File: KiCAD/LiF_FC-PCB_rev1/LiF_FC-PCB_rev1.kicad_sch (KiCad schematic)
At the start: 0 parts

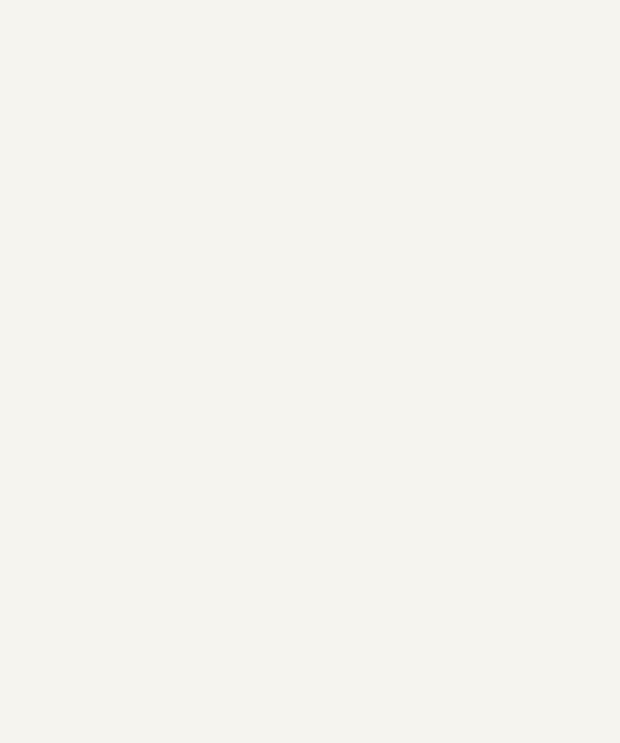
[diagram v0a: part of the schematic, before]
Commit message: merged and fixed Rita's CAN and Load Cell schematics
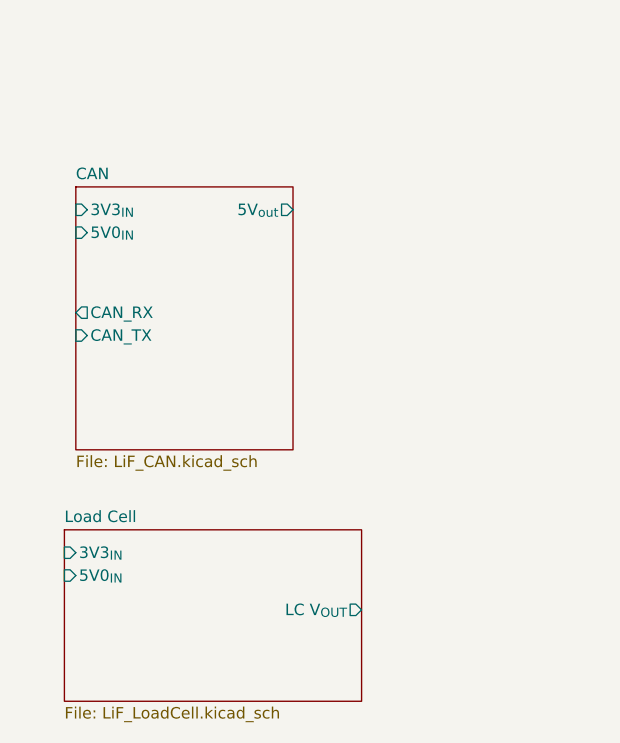
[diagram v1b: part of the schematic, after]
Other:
- added sheet CAN (LiF_CAN.kicad_sch)
- added sheet Load Cell (LiF_LoadCell.kicad_sch)
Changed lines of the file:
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@@
 	(paper "A4")
+	(sheet
+		(at 67.31 171.45)
+		(size 33.02 19.05)
+		(exclude_from_sim no)
+		(in_bom yes)
+		(on_board yes)
+		(dnp no)
+		(fields_autoplaced yes)
+		(stroke
+			(width 0.1524)
+			(type solid)
+		)
+		(fill
+			(color 0 0 0 0.0000)
+		)
+		(property "Sheetname" "Load Cell"
+			(at 67.31 170.7384 0)
+			(effects
+				(font
+					(size 1.27 1.27)
+				)
+				(justify left bottom)
+			)
+		)
+		(property "Sheetfile" "LiF_LoadCell.kicad_sch"
+			(at 67.31 191.0846 0)
+			(effects
+				(font
+					(size 1.27 1.27)
+				)
+				(justify left top)
+			)
+		)
+		(pin "3V3_{IN}" input
+			(at 67.31 173.99 180)
+			(effects
+				(font
+					(size 1.27 1.27)
+				)
+				(justify left)
+			)
+		)
+		(pin "5V0_{IN}" input
+			(at 67.31 176.53 180)
+			(effects
+				(font
+					(size 1.27 1.27)
+				)
+				(justify left)
+			)
+		)
+		(pin "LC V_{OUT}" output
+			(at 100.33 180.34 0)
+			(effects
+				(font
+					(size 1.27 1.27)
+				)
+				(justify right)
+			)
+		)
+		(instances
+			(project "LiF_FC-PCB_rev1"
+				(path "/9e3e8da7-e506-46c9-90e5-307e4ad30d29"
+					(page "7")
+				)
+			)
+		)
+	)
+	(sheet
+		(at 68.58 133.35)
+		(size 24.13 29.21)
+		(exclude_from_sim no)
+		(in_bom yes)
+		(on_board yes)
+		(dnp no)
+		(fields_autoplaced yes)
+		(stroke
+			(width 0.1524)
+			(type solid)
+		)
+		(fill
+			(color 0 0 0 0.0000)
+		)
+		(property "Sheetname" "CAN"
+			(at 68.58 132.6384 0)
+			(effects
+				(font
+					(size 1.27 1.27)
+				)
+				(justify left bottom)
+			)
+		)
+		(property "Sheetfile" "LiF_CAN.kicad_sch"
+			(at 68.58 163.1446 0)
+			(effects
+				(font
+					(size 1.27 1.27)
+				)
+				(justify left top)
+			)
+		)
+		(pin "3V3_{IN}" input
+			(at 68.58 135.89 180)
+			(effects
+				(font
+					(size 1.27 1.27)
+				)
+				(justify left)
+			)
+		)
+		(pin "5V0_{IN}" input
+			(at 68.58 138.43 180)
+			(effects
+				(font
+					(size 1.27 1.27)
+				)
+				(justify left)
+			)
+		)
+		(pin "5V_{out}" output
+			(at 92.71 135.89 0)
+			(effects
+				(font
+					(size 1.27 1.27)
+				)
+				(justify right)
+			)
+		)
+		(pin "CAN_RX" output
+			(at 68.58 147.32 180)
+			(effects
+				(font
+					(size 1.27 1.27)
+				)
+				(justify left)
+			)
+		)
+		(pin "CAN_TX" input
+			(at 68.58 149.86 180)
+			(effects
+				(font
+					(size 1.27 1.27)
+				)
+				(justify left)
+			)
+		)
+		(instances
+			(project "LiF_FC-PCB_rev1"
+				(path "/9e3e8da7-e506-46c9-90e5-307e4ad30d29"
+					(page "6")
+				)
+			)
+		)
+	)
 	(sheet
 		(at 193.04 100.33)

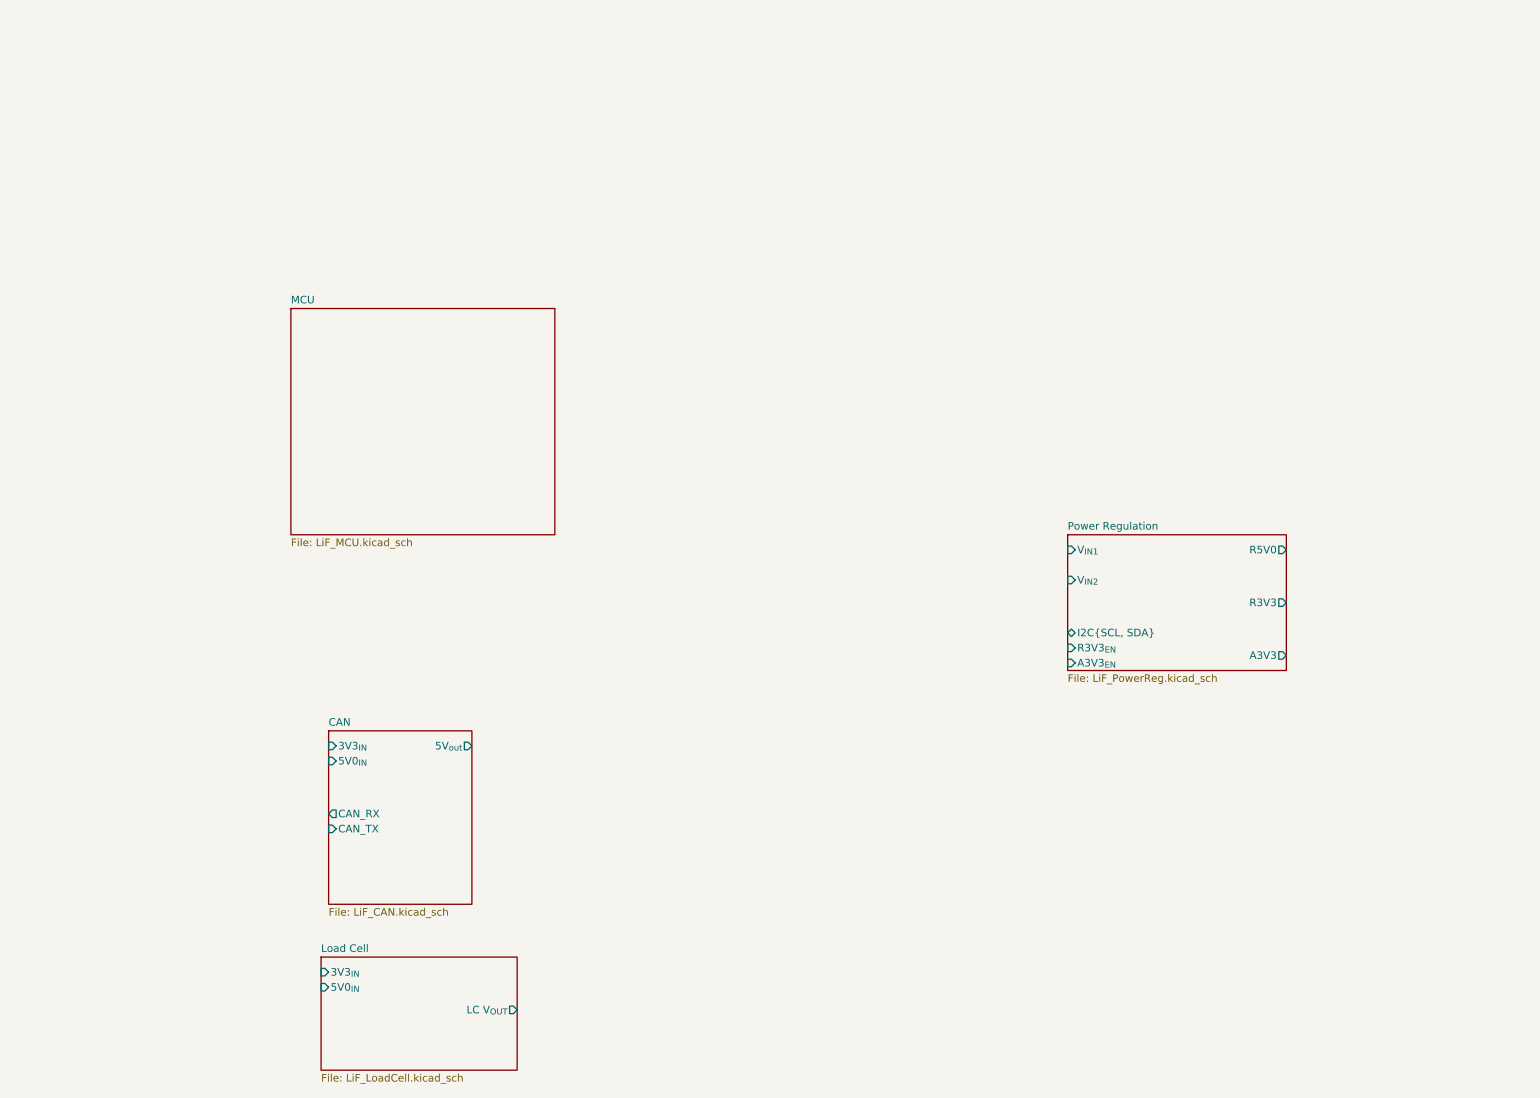
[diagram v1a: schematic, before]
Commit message: reverted 5V reg, reworked power distribution logic, swapped power OR-ing ICs
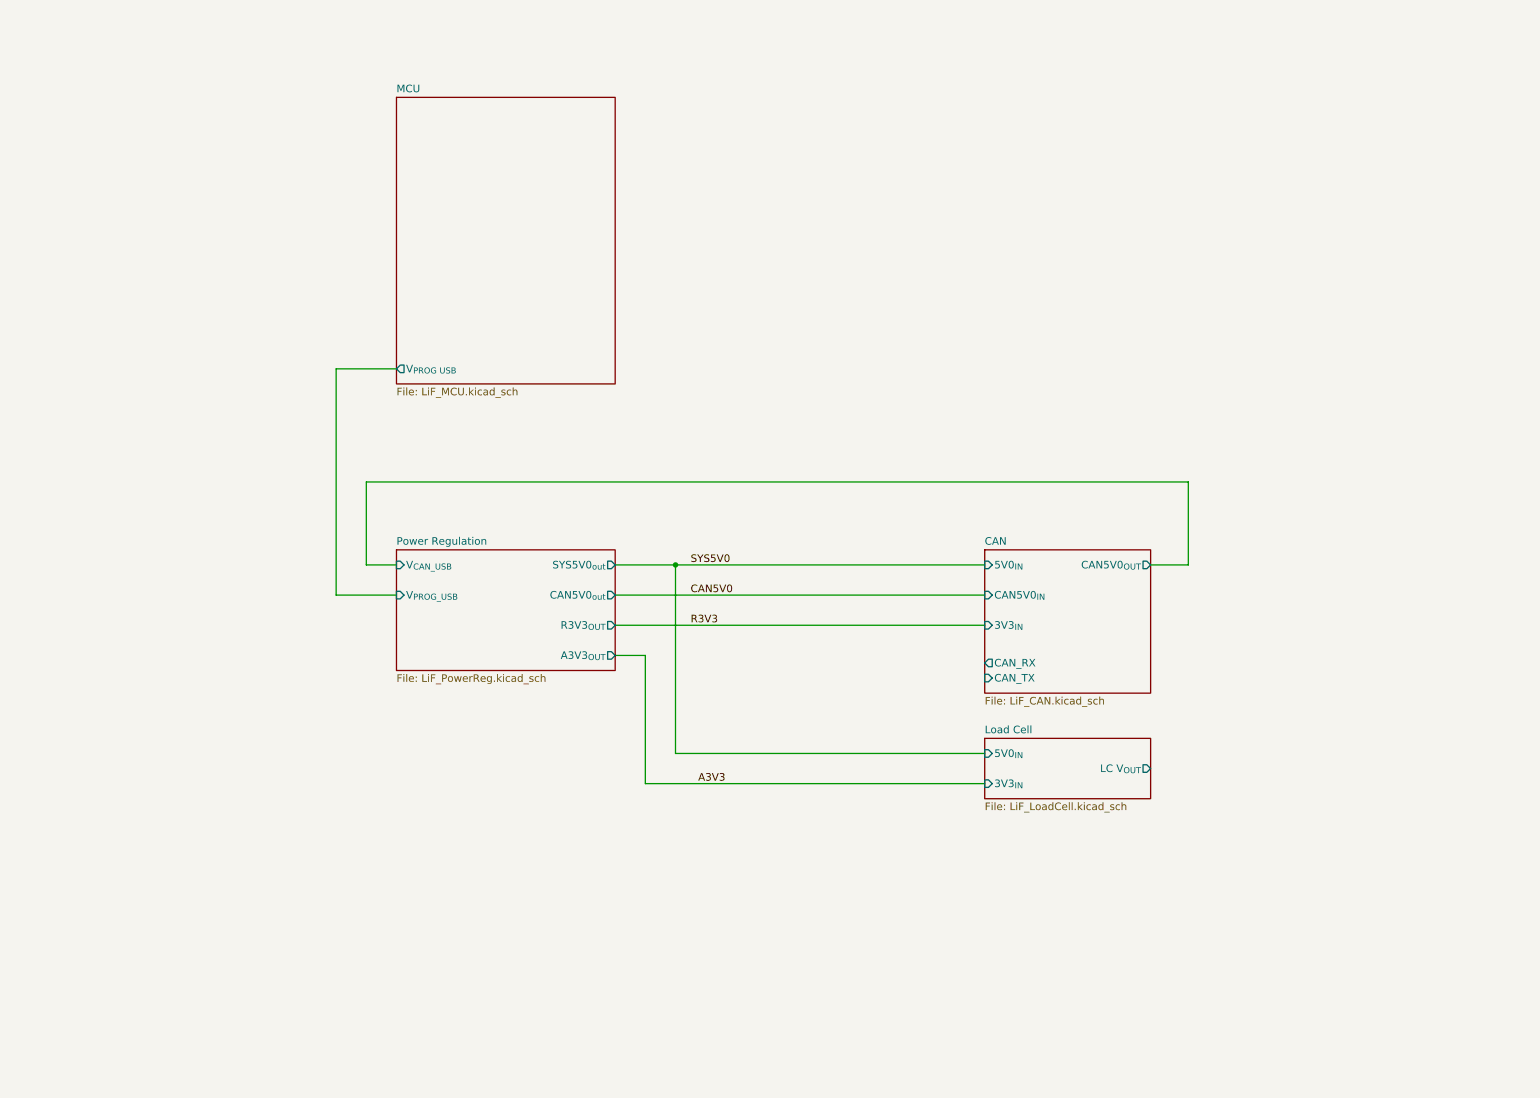
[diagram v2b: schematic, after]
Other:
- sheet CAN ports: added CAN5V0_{IN}, CAN5V0_{OUT}; removed 5V_{out}
- sheet MCU ports: added V_{PROG USB}; removed none
- sheet Power Regulation ports: added A3V3_{OUT}, CAN5V0_{out}, R3V3_{OUT}, SYS5V0_{out}, V_{CAN_USB}, V_{PROG_USB}; removed A3V3, A3V3_{EN}, I2C{SCL, SDA}, R3V3, R3V3_{EN}, R5V0, V_{IN1}, V_{IN2}

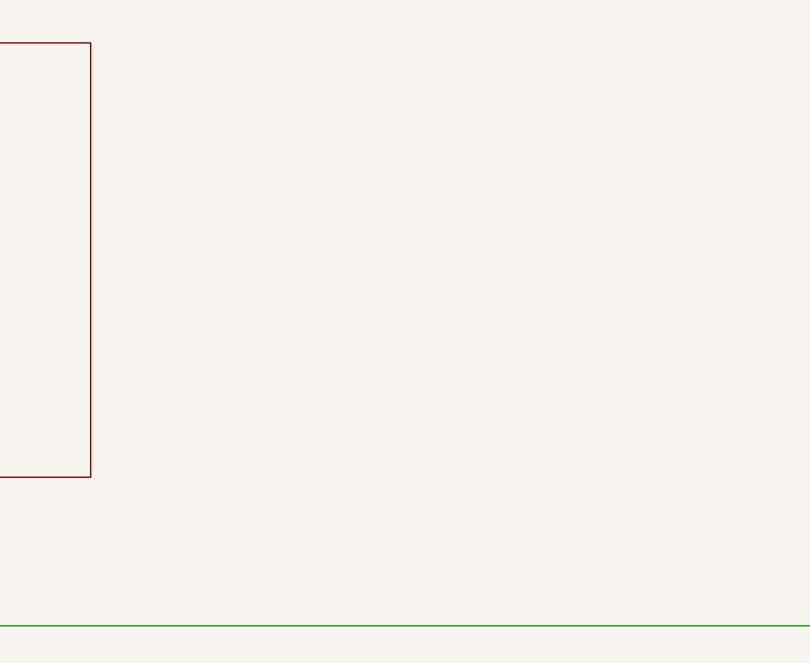
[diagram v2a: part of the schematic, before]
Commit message: starting to merge Nick's schematics into the main KiCAD project
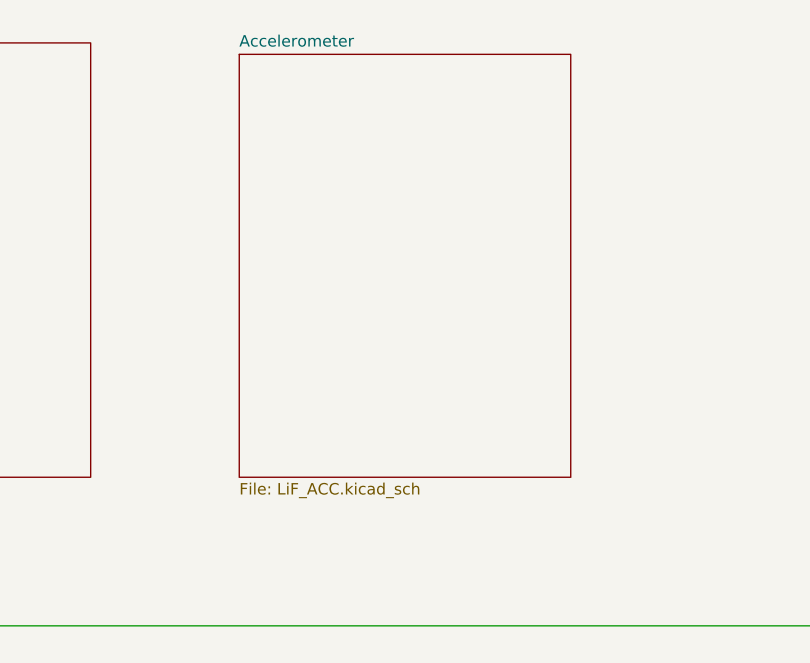
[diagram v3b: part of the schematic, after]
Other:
- added sheet Accelerometer (LiF_ACC.kicad_sch)
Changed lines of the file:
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@@
+	)
+	(sheet
+		(at 133.35 27.94)
+		(size 36.83 46.99)
+		(exclude_from_sim no)
+		(in_bom yes)
+		(on_board yes)
+		(dnp no)
+		(fields_autoplaced yes)
+		(stroke
+			(width 0.1524)
+			(type solid)
+		)
+		(fill
+			(color 0 0 0 0.0000)
+		)
+		(property "Sheetname" "Accelerometer"
+			(at 133.35 27.2284 0)
+			(effects
+				(font
+					(size 1.27 1.27)
+				)
+				(justify left bottom)
+			)
+		)
+		(property "Sheetfile" "LiF_ACC.kicad_sch"
+			(at 133.35 75.5146 0)
+			(effects
+				(font
+					(size 1.27 1.27)
+				)
+				(justify left top)
+			)
+		)
+		(instances
+			(project "LiF_FC-PCB_rev1"
+				(path "/9e3e8da7-e506-46c9-90e5-307e4ad30d29"
+					(page "9")
+				)
+			)
+		)
 	)
 	(sheet

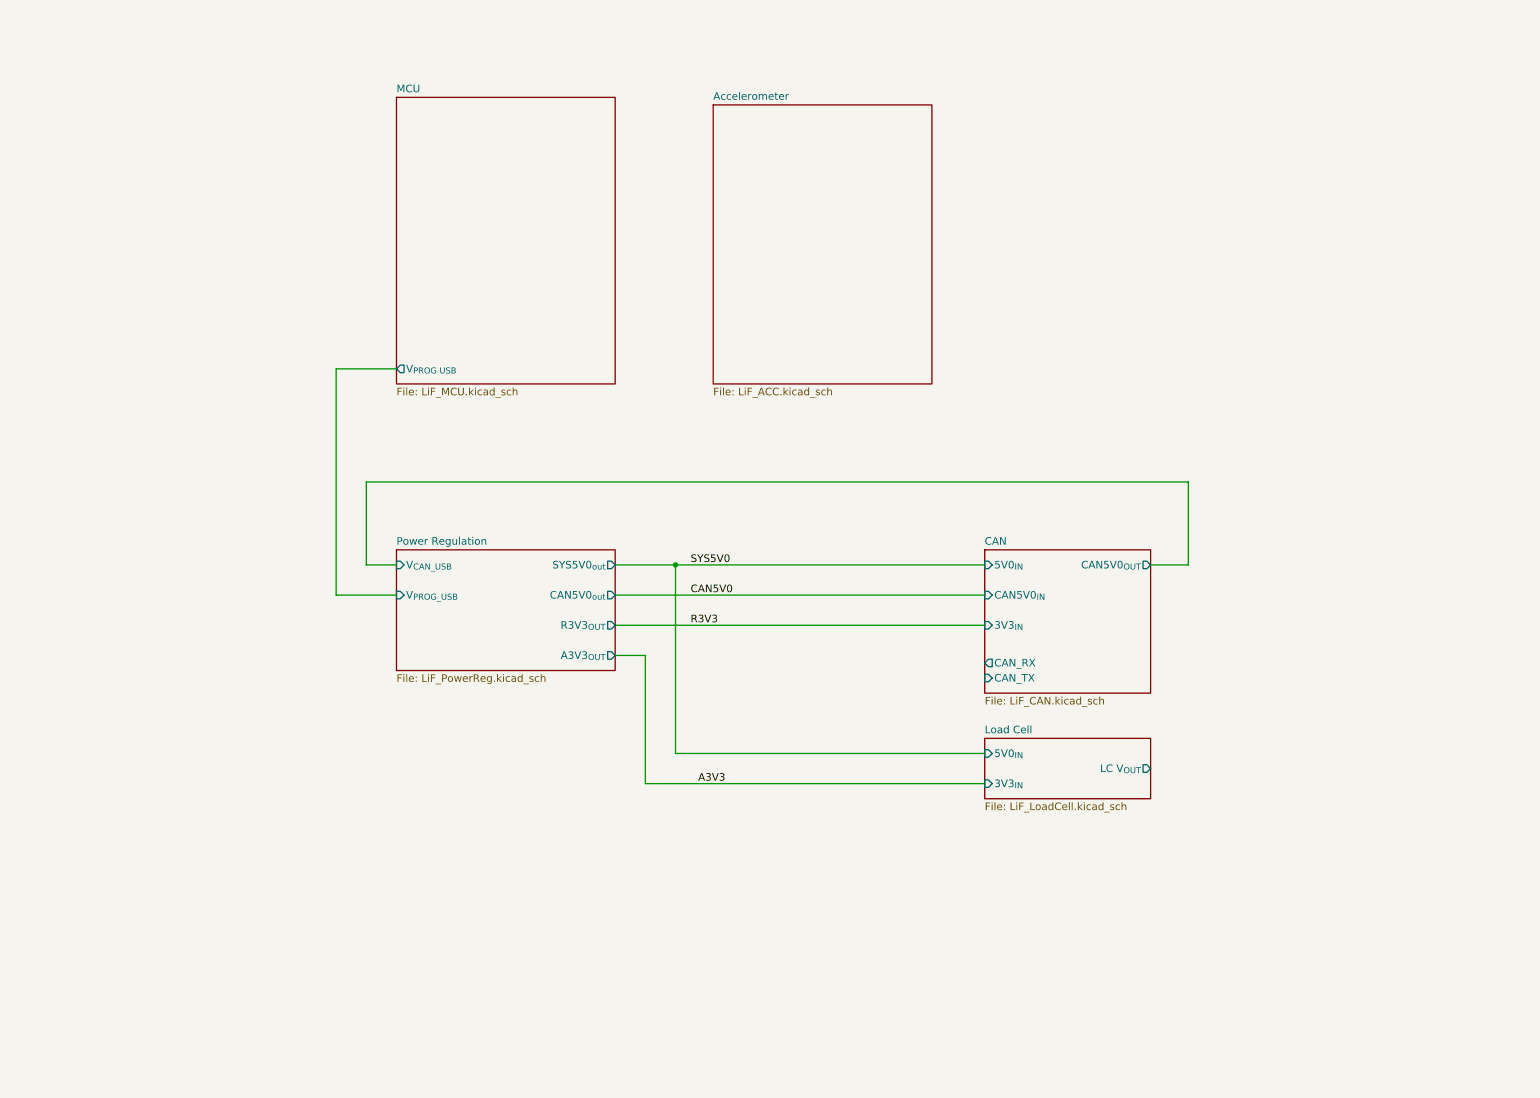
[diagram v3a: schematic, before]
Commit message: Finished schematics, mostly. Only MCU sheet left. Doing component sourcing
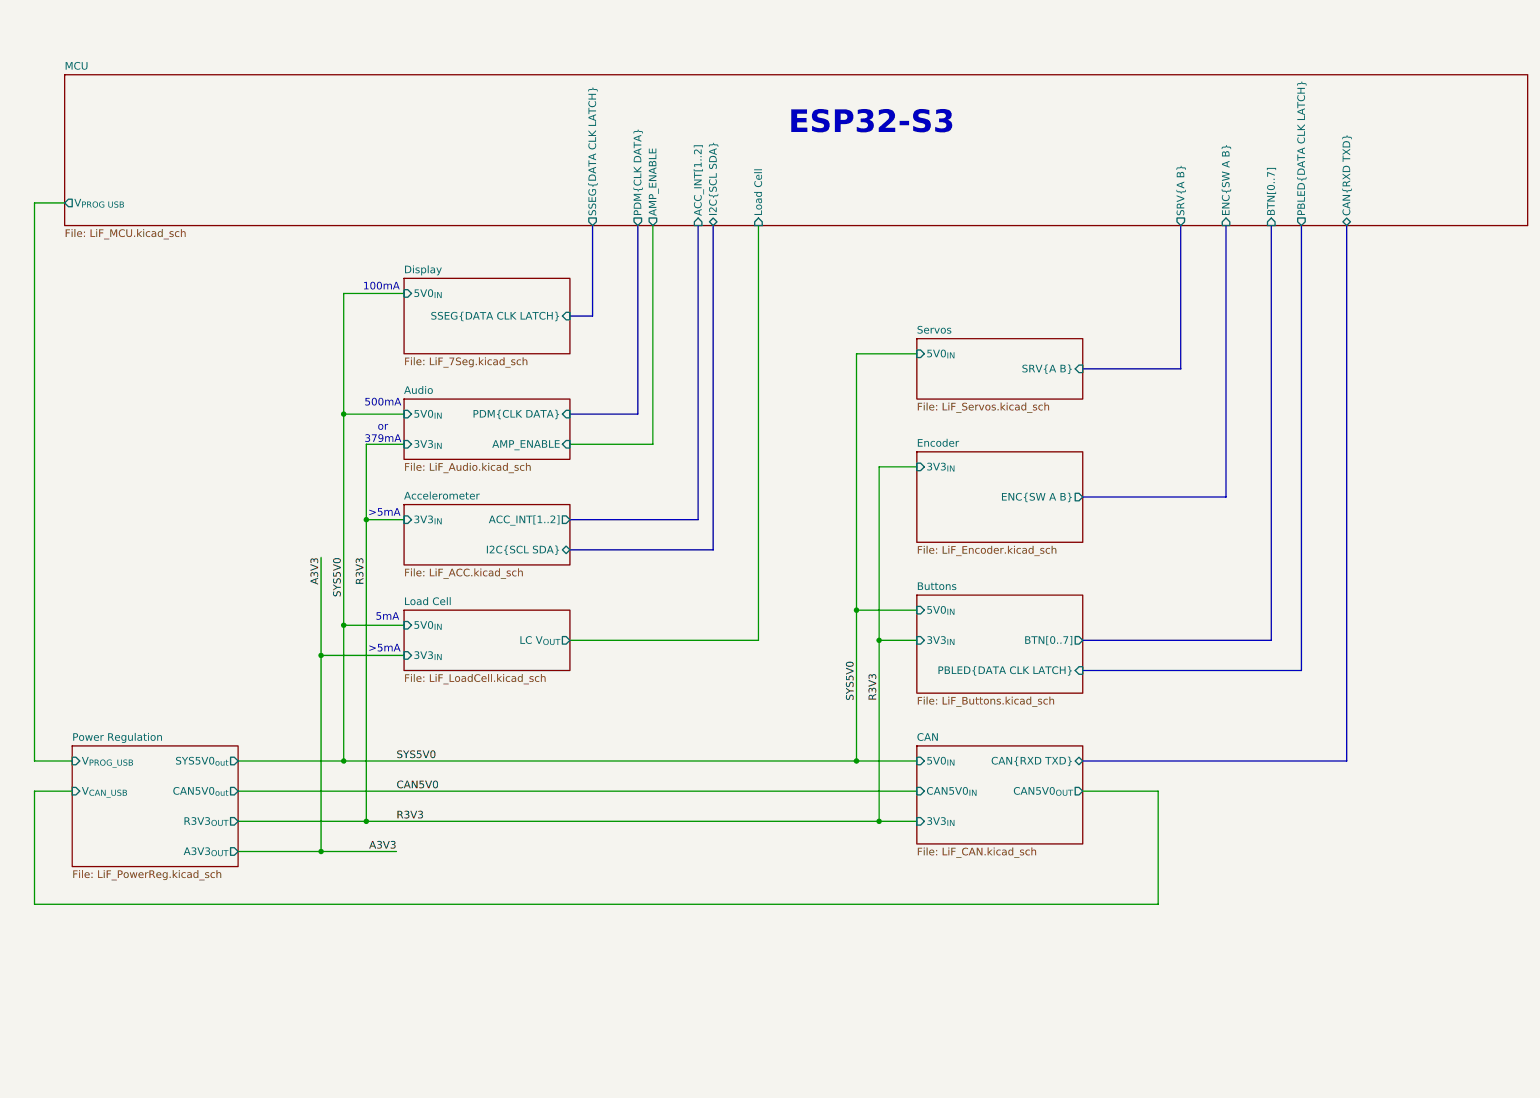
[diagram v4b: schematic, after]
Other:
- added sheet Audio (LiF_Audio.kicad_sch)
- added sheet Buttons (LiF_Buttons.kicad_sch)
- added sheet Display (LiF_7Seg.kicad_sch)
- added sheet Encoder (LiF_Encoder.kicad_sch)
- added sheet Servos (LiF_Servos.kicad_sch)
- sheet Accelerometer ports: added 3V3_{IN}, ACC_INT[1..2], I2C{SCL SDA}; removed none
- sheet CAN ports: added CAN{RXD TXD}; removed CAN_RX, CAN_TX
- sheet MCU ports: added ACC_INT[1..2], AMP_ENABLE, BTN[0..7], CAN{RXD TXD}, ENC{SW A B}, I2C{SCL SDA}, Load Cell, PBLED{DATA CLK LATCH}, PDM{CLK DATA}, SRV{A B}, SSEG{DATA CLK LATCH}; removed none
- note added: "100mA"
- note added: "500mA or 379mA"
- note added: "5mA"
- note added: ">5mA"
- note added: "ESP32-S3"
- company: (none) -> Lithium Firefly Team
